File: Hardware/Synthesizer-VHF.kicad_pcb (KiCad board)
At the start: 4 copper layers, 38.9 x 37.7 mm, 85 parts, among them J1 Screw_Terminal_01x02, J2 Scope, J4 USB-C 2.0 16P, J5 REF_IN, J6 Scope, J7 RFOUTA, J8 Header 1x3, J9 RFOUTB, U1 LM7805A, U2 FT231XQ, U3 ATtiny1616-M, U4 ADF4351, U7 ADP150AUJZ-3.3-R7, U8 ADP150AUJZ-3.3-R7, X1 HCI 8122S-25NQ33FTL

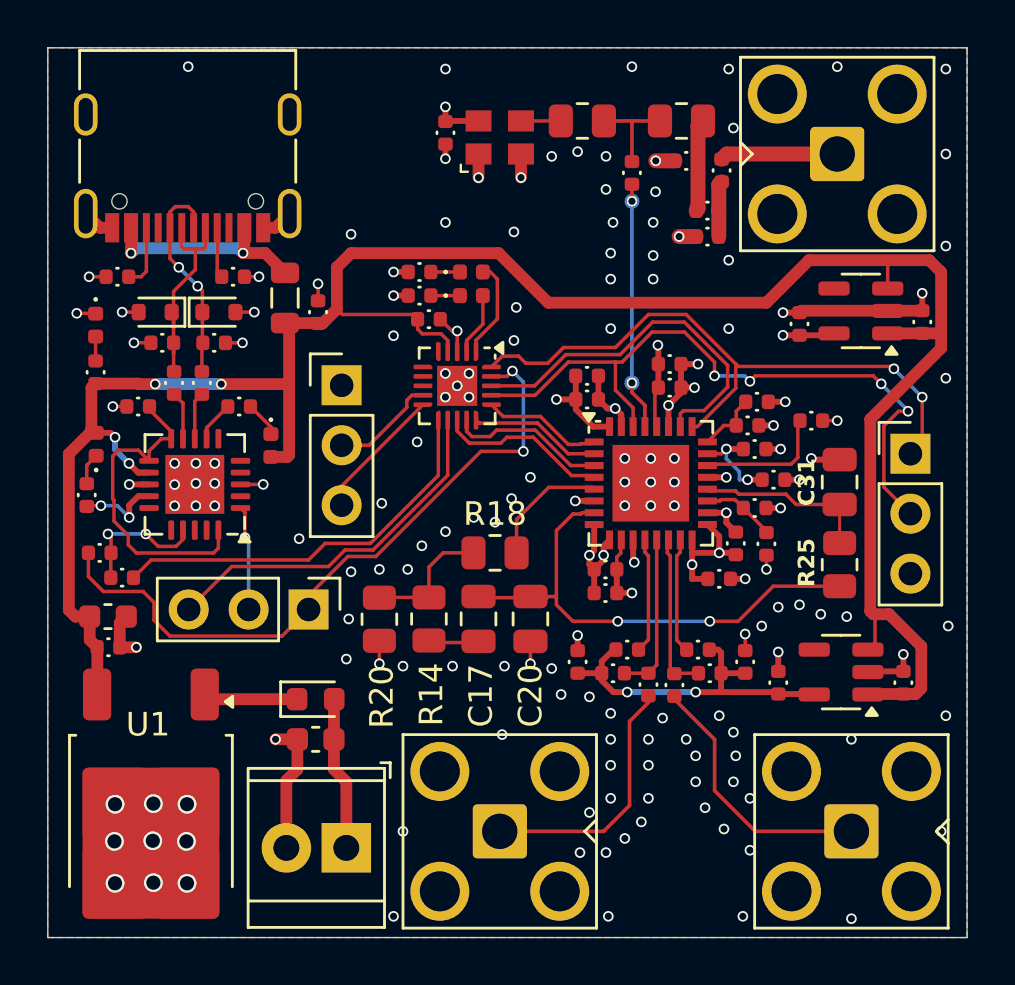
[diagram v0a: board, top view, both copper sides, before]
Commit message: Adding userinterface for configuring synth
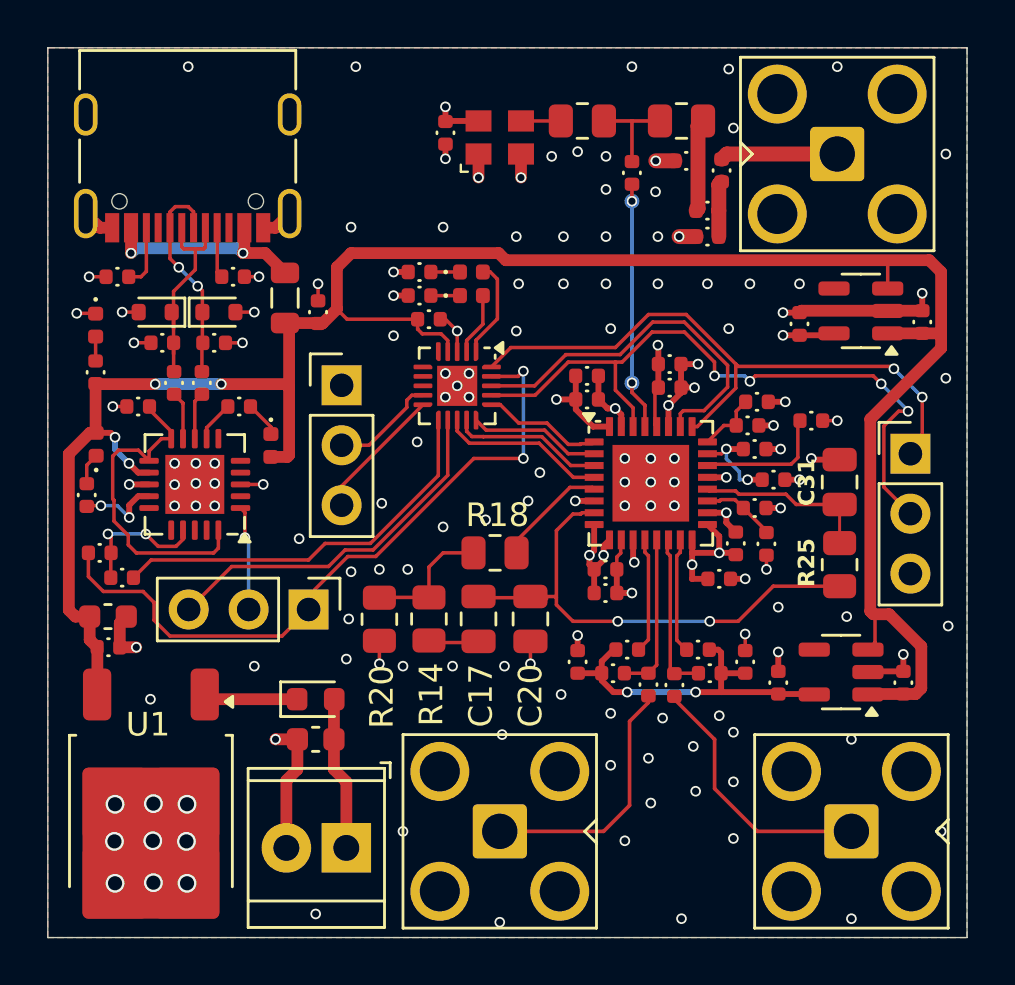
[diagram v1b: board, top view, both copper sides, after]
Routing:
- net /5V: track 98.3 -> 96.7 mm
- net Net-(U4-SW): track 5.30 -> 4.77 mm
- net GND: vias 168 -> 150
